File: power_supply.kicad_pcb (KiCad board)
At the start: 2 copper layers, 66.3 x 45.5 mm, 21 parts, among them J1 Screw_Terminal_01x02, J2 Conn_01x03_Pin, J3 Jack-DC, SW1 SW_Push_DPDT, T1 TY-311P, U1 LM7805_TO220, U2 LM317L_SOT-89

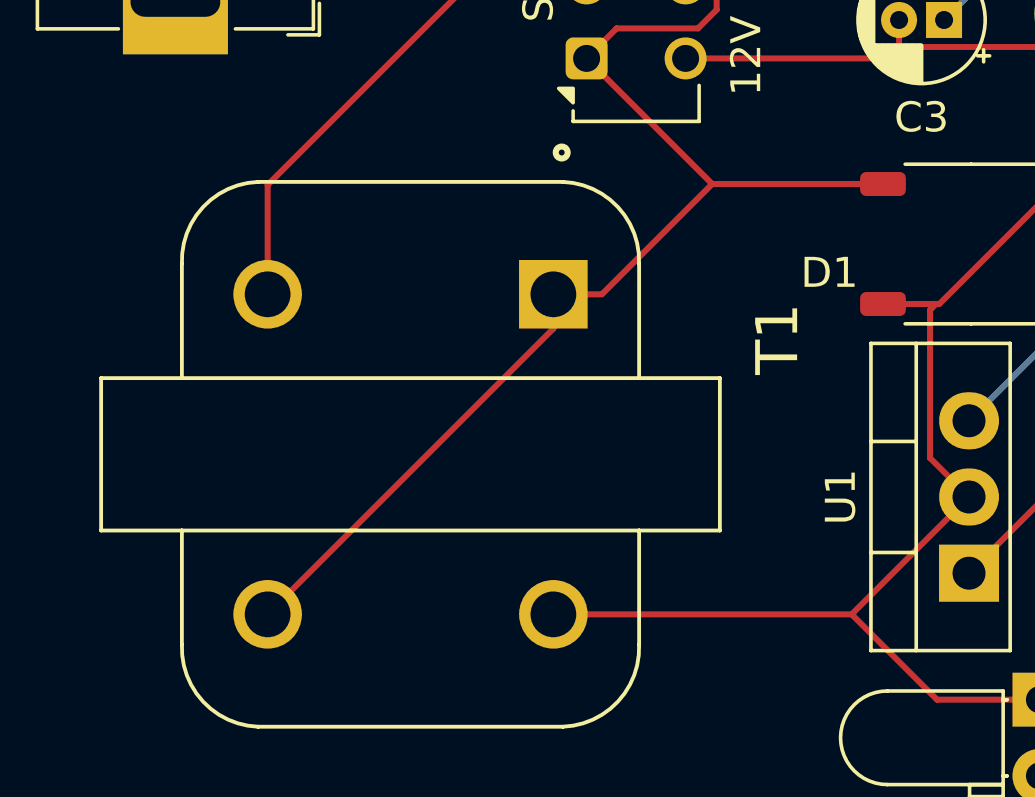
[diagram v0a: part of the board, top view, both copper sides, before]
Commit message: modified some tracks
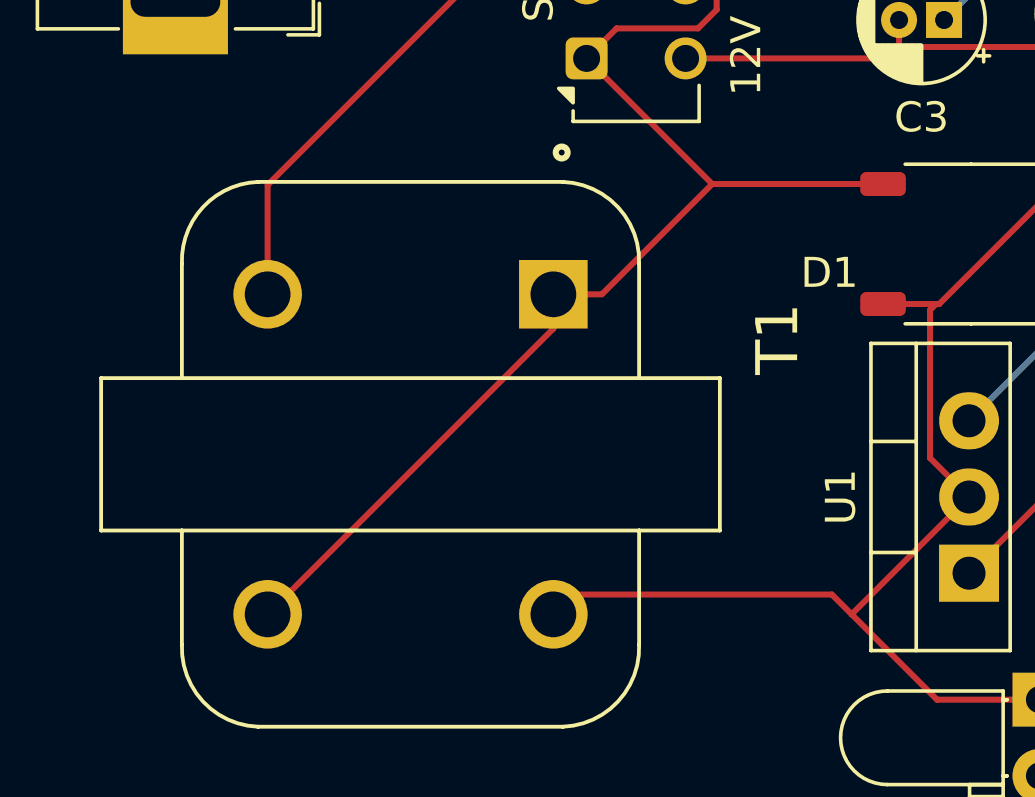
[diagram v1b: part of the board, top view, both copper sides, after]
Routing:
- net GND: track 90.3 -> 90.8 mm
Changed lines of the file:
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@@
 			(viasonmask no)
 			(mode 1)
-			(useauxorigin no)
+			(useauxorigin yes)
 			(hpglpennumber 1)
 			(hpglpenspeed 20)
@@
 			(outputformat 1)
 			(mirror no)
-			(drillshape 1)
+			(drillshape 0)
 			(scaleselection 1)
 			(outputdirectory "")
@@
 		(tags "TSSOP SO")
 		(property "Reference" "D1"
-			(at 4.7244 -0.9652 360)
+			(at 4.7244 -0.9652 0)
 			(layer "F.SilkS")
 			(effects
@@
 		)
 		(property "Value" "MDB10S"
-			(at 0 3.45 360)
+			(at 0 3.45 0)
 			(layer "F.Fab")
 			(effects
@@
 		)
 		(property "Footprint" "Package_SO:TSSOP-4_4.4x5mm_P4mm"
-			(at 0 0 360)
+			(at 0 0 0)
 			(layer "F.Fab")
 			(hide yes)
@@
 		)
 		(property "Datasheet" "https://www.onsemi.com/pub/Collateral/MDB8S-D.PDF"
-			(at 0 0 360)
+			(at 0 0 0)
 			(layer "F.Fab")
 			(hide yes)
@@
 		)
 		(property "Description" "Single-Phase Bridge Rectifier, 700V Vrms, 1A If, TSSOP-4"
-			(at 0 0 360)
+			(at 0 0 0)
 			(layer "F.Fab")
 			(hide yes)
@@
 		)
 		(fp_text user "${REFERENCE}"
-			(at 0 0 360)
+			(at 0 0 0)
 			(layer "F.Fab")
 			(effects
@@
 		(tags "CP Radial series Radial pin pitch 1.50mm  diameter 4mm Electrolytic Capacitor")
 		(property "Reference" "C2"
-			(at 0.75 -3.25 360)
+			(at 0.75 -3.25 0)
 			(layer "F.SilkS")
 			(effects
@@
 		)
 		(property "Value" "C_Polarized"
-			(at 0.75 3.25 360)
+			(at 0.75 3.25 0)
 			(layer "F.Fab")
 			(effects
@@
 		)
 		(fp_text user "${REFERENCE}"
-			(at 0.75 0 360)
+			(at 0.75 0 0)
 			(layer "F.Fab")
 			(effects
@@
 		)
 		(fp_text user "${REFERENCE}"
-			(at 0 1 360)
+			(at 0 1 0)
 			(layer "F.Fab")
 			(effects
@@
 		)
 		(fp_text user "${REFERENCE}"
-			(at 0.2 0 360)
+			(at 0.2 0 0)
 			(layer "F.Fab")
 			(effects
@@
 		(tags "CP Radial series Radial pin pitch 1.50mm  diameter 4mm Electrolytic Capacitor")
 		(property "Reference" "C1"
-			(at 0.75 -3.25 360)
+			(at 0.75 -3.25 0)
 			(layer "F.SilkS")
 			(effects
@@
 		)
 		(property "Value" "C_Polarized"
-			(at 0.75 3.25 360)
+			(at 0.75 3.25 0)
 			(layer "F.Fab")
 			(effects
@@
 		)
 		(fp_text user "${REFERENCE}"
-			(at 0.75 0 360)
+			(at 0.75 0 0)
 			(layer "F.Fab")
 			(effects
@@
 		(fp_arc
 			(start -6.35 7.62)
-			(mid -8.241301 6.915505)
+			(mid -8.241302 6.915505)
 			(end -9.0805 5.08)
 			(stroke
@@
 		(fp_arc
 			(start -6.35 7.62)
-			(mid -8.241301 6.915505)
+			(mid -8.241302 6.915505)
 			(end -9.0805 5.08)
 			(stroke
@@
 		(fp_arc
 			(start -6.35 7.62)
-			(mid -8.241301 6.915505)
+			(mid -8.241302 6.915505)
 			(end -9.0805 5.08)
 			(stroke
@@
 		(fp_arc
 			(start -6.35 7.62)
-			(mid -8.241301 6.915505)
+			(mid -8.241302 6.915505)
 			(end -9.0805 5.08)
 			(stroke
@@
 		(fp_arc
 			(start -9.0805 -5.08)
-			(mid -8.241301 -6.915505)
+			(mid -8.241301 -6.915504)
 			(end -6.35 -7.62)
 			(stroke
@@
 		(fp_arc
 			(start -9.0805 -5.08)
-			(mid -8.241301 -6.915505)
+			(mid -8.241301 -6.915504)
 			(end -6.35 -7.62)
 			(stroke
@@
 		(fp_arc
 			(start -9.0805 -5.08)
-			(mid -8.241301 -6.915505)
+			(mid -8.241301 -6.915504)
 			(end -6.35 -7.62)
 			(stroke
@@
 		(fp_arc
 			(start -9.0805 -5.08)
-			(mid -8.241301 -6.915505)
+			(mid -8.241301 -6.915504)
 			(end -6.35 -7.62)
 			(stroke
@@
 		(fp_arc
 			(start -6.35 7.62)
-			(mid -8.241301 6.915505)
+			(mid -8.241302 6.915505)
 			(end -9.0805 5.08)
 			(stroke
@@
 		(fp_arc
 			(start -6.35 7.62)
-			(mid -8.241301 6.915505)
+			(mid -8.241302 6.915505)
 			(end -9.0805 5.08)
 			(stroke
@@
 		(fp_arc
 			(start -6.35 7.62)
-			(mid -8.241301 6.915505)
+			(mid -8.241302 6.915505)
 			(end -9.0805 5.08)
 			(stroke
@@
 		(fp_arc
 			(start -6.35 7.62)
-			(mid -8.241301 6.915505)
+			(mid -8.241302 6.915505)
 			(end -9.0805 5.08)
 			(stroke
@@
 		(fp_arc
 			(start -9.0805 -5.08)
-			(mid -8.241301 -6.915505)
+			(mid -8.241301 -6.915504)
 			(end -6.35 -7.62)
 			(stroke
@@
 		(fp_arc
 			(start -9.0805 -5.08)
-			(mid -8.241301 -6.915505)
+			(mid -8.241301 -6.915504)
 			(end -6.35 -7.62)
 			(stroke
@@
 		(fp_arc
 			(start -9.0805 -5.08)
-			(mid -8.241301 -6.915505)
+			(mid -8.241301 -6.915504)
 			(end -6.35 -7.62)
 			(stroke
@@
 		(fp_arc
 			(start -9.0805 -5.08)
-			(mid -8.241301 -6.915505)
+			(mid -8.241301 -6.915504)
 			(end -6.35 -7.62)
 			(stroke
@@
 		(tags "Resistor Axial_DIN0207 series Axial Horizontal pin pitch 7.62mm 0.25W = 1/4W length 6.3mm diameter 2.5mm")
 		(property "Reference" "R1"
-			(at 3.81 -2.37 360)
+			(at 3.81 -2.37 0)
 			(layer "F.SilkS")
 			(effects
@@
 		)
 		(property "Value" "R"
-			(at 3.81 2.37 360)
+			(at 3.81 2.37 0)
 			(layer "F.Fab")
 			(effects
@@
 		)
 		(fp_text user "${REFERENCE}"
-			(at 3.81 0 360)
+			(at 3.81 0 0)
 			(layer "F.Fab")
 			(effects
@@
 		(tags "Resistor Axial_DIN0207 series Axial Horizontal pin pitch 7.62mm 0.25W = 1/4W length 6.3mm diameter 2.5mm")
 		(property "Reference" "R3"
-			(at 3.81 -2.37 360)
+			(at 3.81 -2.37 0)
 			(layer "F.SilkS")
 			(effects
@@
 		)
 		(property "Value" "R"
-			(at 3.81 2.37 360)
+			(at 3.81 2.37 0)
 			(layer "F.Fab")
 			(effects
@@
 		)
 		(fp_text user "${REFERENCE}"
-			(at 3.81 0 360)
+			(at 3.81 0 0)
 			(layer "F.Fab")
 			(effects
@@
 		(tags "THT Terminal Block Phoenix MKDS-1,5-2-5.08 pitch 5.08mm size 10.2x9.8mm^2 drill 1.3mm pad 2.6mm")
 		(property "Reference" "J1"
-			(at 2.54 -6.26 360)
+			(at 2.54 -6.26 0)
 			(layer "F.SilkS")
 			(effects
@@
 		)
 		(fp_text user "${REFERENCE}"
-			(at 2.54 3.2 360)
+			(at 2.54 3.2 0)
 			(layer "F.Fab")
 			(effects
@@
 		(tags "CP Radial series Radial pin pitch 1.50mm  diameter 4mm Electrolytic Capacitor")
 		(property "Reference" "C3"
-			(at 0.75 -3.25 360)
+			(at 0.75 -3.25 0)
 			(layer "F.SilkS")
 			(effects
@@
 		)
 		(property "Value" "C_Polarized"
-			(at 0.75 3.25 360)
+			(at 0.75 3.25 0)
 			(layer "F.Fab")
 			(effects
@@
 		)
 		(fp_text user "${REFERENCE}"
-			(at 0.75 0 360)
+			(at 0.75 0 0)
 			(layer "F.Fab")
 			(effects
@@
 		(at 153.6192 64.77 180)
 		(property "Reference" "G***"
-			(at 0 0 360)
+			(at 0 0 0)
 			(layer "F.SilkS")
 			(hide yes)
@@
 		)
 		(property "Value" "LOGO"
-			(at 0.75 0 360)
+			(at 0.75 0 0)
 			(layer "F.SilkS")
 			(hide yes)
@@
 		)
 		(property "Footprint" "logos:eagle"
-			(at 0 0 360)
+			(at 0 0 0)
 			(layer "F.Fab")
 			(hide yes)
@@
 		)
 		(property "Datasheet" ""
-			(at 0 0 360)
+			(at 0 0 0)
 			(layer "F.Fab")
 			(hide yes)
@@
 		)
 		(property "Description" ""
-			(at 0 0 360)
+			(at 0 0 0)
 			(layer "F.Fab")
 			(hide yes)
@@
 	)
 	(segment
+		(start 150.86905 97.6884)
+		(end 159.4918 97.6884)
+		(width 0.2)
+		(layer "F.Cu")
+		(net 1)
+	)
+	(segment
+		(start 159.4918 97.6884)
+		(end 160.1522 98.3488)
+		(width 0.2)
+		(layer "F.Cu")
+		(net 1)
+	)
+	(segment
 		(start 162.7638 88.207)
 		(end 162.9664 88.0044)
@@
 	)
 	(segment
-		(start 150.20865 98.3488)
-		(end 160.1522 98.3488)
+		(start 173.619 78.2828)
+		(end 172.8698 77.5336)
 		(width 0.2)
 		(layer "F.Cu")
@@
 	)
 	(segment
-		(start 173.619 78.2828)
-		(end 172.8698 77.5336)
+		(start 150.20865 98.3488)
+		(end 150.86905 97.6884)
 		(width 0.2)
 		(layer "F.Cu")

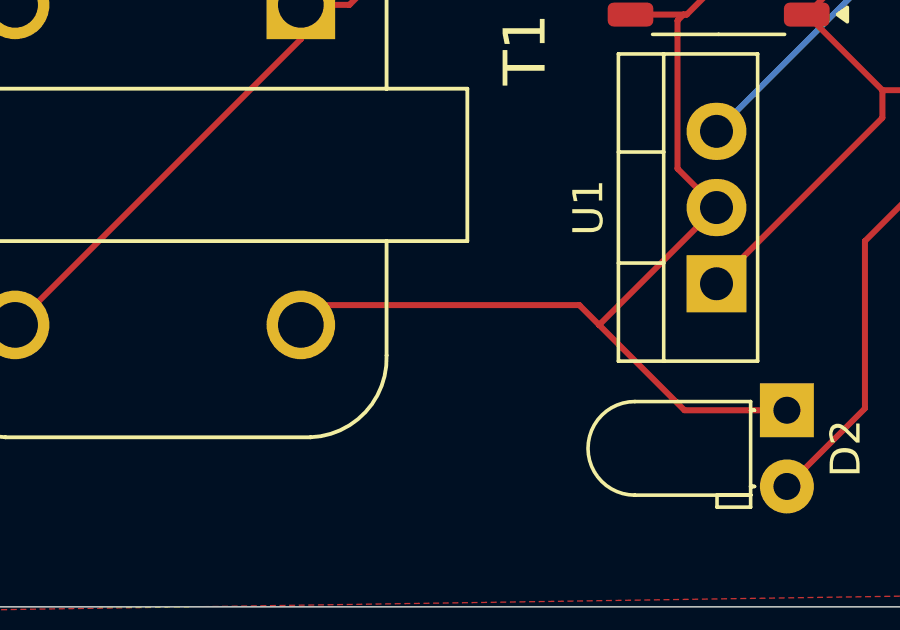
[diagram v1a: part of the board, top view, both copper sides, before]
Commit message: added schematic as a PDF
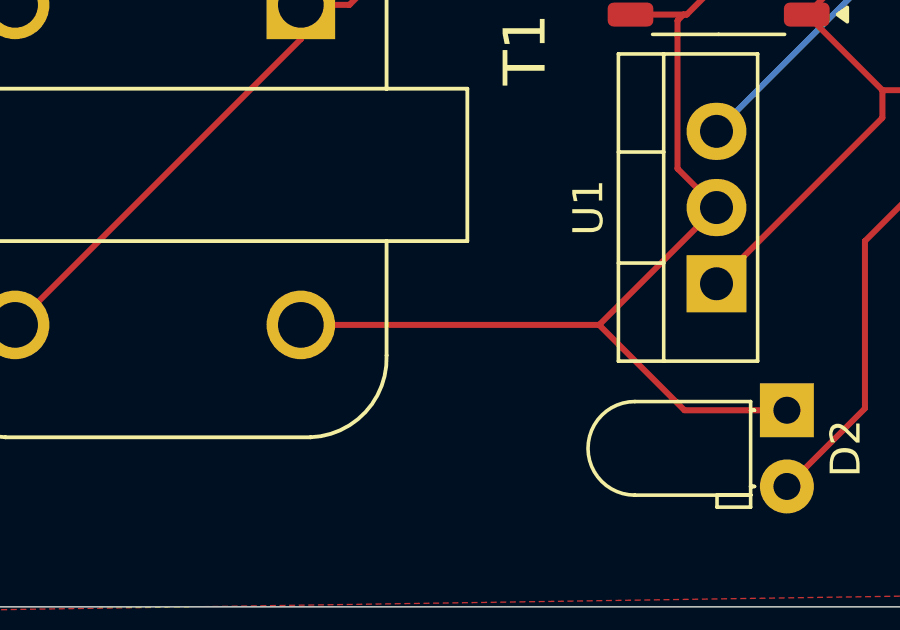
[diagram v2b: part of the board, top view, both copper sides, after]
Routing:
- net GND: track 90.8 -> 90.3 mm
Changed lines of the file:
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@@
-	)
-	(segment
-		(start 150.86905 97.6884)
-		(end 159.4918 97.6884)
-		(width 0.2)
-		(layer "F.Cu")
-		(net 1)
-	)
-	(segment
-		(start 159.4918 97.6884)
-		(end 160.1522 98.3488)
-		(width 0.2)
-		(layer "F.Cu")
-		(net 1)
 	)
 	(segment
@@
 	)
 	(segment
-		(start 173.619 78.2828)
-		(end 172.8698 77.5336)
+		(start 150.20865 98.3488)
+		(end 160.1522 98.3488)
 		(width 0.2)
 		(layer "F.Cu")
@@
 	)
 	(segment
-		(start 150.20865 98.3488)
-		(end 150.86905 97.6884)
+		(start 173.619 78.2828)
+		(end 172.8698 77.5336)
 		(width 0.2)
 		(layer "F.Cu")
